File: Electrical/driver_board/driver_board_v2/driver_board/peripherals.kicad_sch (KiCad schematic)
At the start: 16 parts, among them J10 Conn_01x02_Socket, J11 Conn_01x06_Pin

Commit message: Value assignment and protection for driver board
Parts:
- renumbered C43 to C44, C44 to C45, C45 to C46, C46 to C47, C47 to C48, C48 to C49, C49 to C50, C50 to C51, J11 to J10, J10 to J11

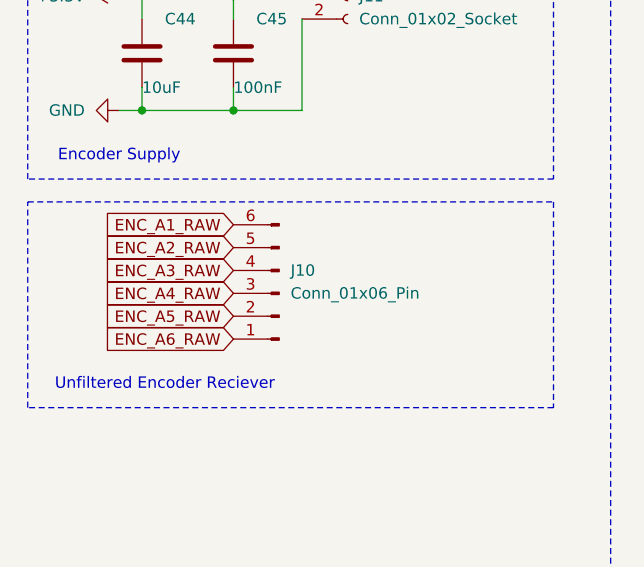
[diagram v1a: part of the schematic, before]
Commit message: Improved routing
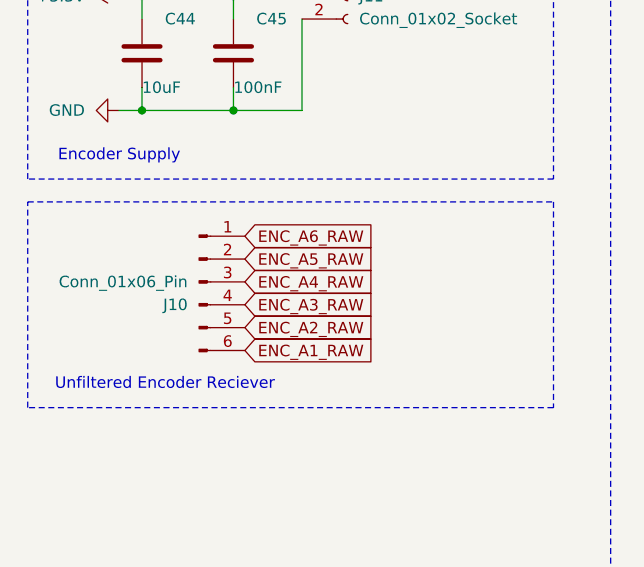
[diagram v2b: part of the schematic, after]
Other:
- moved on the sheet: J10
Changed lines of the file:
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@@
 	(global_label "ENC_A5_RAW"
 		(shape input)
-		(at 63.5 68.58 180)
+		(at 64.77 62.23 0)
 		(fields_autoplaced yes)
 		(effects
@@
 				(size 1.27 1.27)
 			)
-			(justify right)
+			(justify left)
 		)
 		(property "Intersheetrefs" "${INTERSHEET_REFS}"
-			(at 48.722 68.58 0)
-			(hide yes)
-			(show_name no)
-			(do_not_autoplace no)
-			(effects
-				(font
-					(size 1.27 1.27)
-				)
-				(justify right)
+			(at 79.548 62.23 0)
+			(hide yes)
+			(show_name no)
+			(do_not_autoplace no)
+			(effects
+				(font
+					(size 1.27 1.27)
+				)
+				(justify left)
 			)
 		)
@@
 	(global_label "ENC_A2_RAW"
 		(shape input)
-		(at 63.5 60.96 180)
+		(at 64.77 69.85 0)
 		(fields_autoplaced yes)
 		(effects
@@
 				(size 1.27 1.27)
 			)
-			(justify right)
+			(justify left)
 		)
 		(property "Intersheetrefs" "${INTERSHEET_REFS}"
-			(at 48.722 60.96 0)
-			(hide yes)
-			(show_name no)
-			(do_not_autoplace no)
-			(effects
-				(font
-					(size 1.27 1.27)
-				)
-				(justify right)
+			(at 79.548 69.85 0)
+			(hide yes)
+			(show_name no)
+			(do_not_autoplace no)
+			(effects
+				(font
+					(size 1.27 1.27)
+				)
+				(justify left)
 			)
 		)
@@
 	(global_label "ENC_A1_RAW"
 		(shape input)
-		(at 63.5 58.42 180)
+		(at 64.77 72.39 0)
 		(fields_autoplaced yes)
 		(effects
@@
 				(size 1.27 1.27)
 			)
-			(justify right)
+			(justify left)
 		)
 		(property "Intersheetrefs" "${INTERSHEET_REFS}"
-			(at 48.722 58.42 0)
-			(hide yes)
-			(show_name no)
-			(do_not_autoplace no)
-			(effects
-				(font
-					(size 1.27 1.27)
-				)
-				(justify right)
+			(at 79.548 72.39 0)
+			(hide yes)
+			(show_name no)
+			(do_not_autoplace no)
+			(effects
+				(font
+					(size 1.27 1.27)
+				)
+				(justify left)
 			)
 		)
@@
 	(global_label "ENC_A4_RAW"
 		(shape input)
-		(at 63.5 66.04 180)
+		(at 64.77 64.77 0)
 		(fields_autoplaced yes)
 		(effects
@@
 				(size 1.27 1.27)
 			)
-			(justify right)
+			(justify left)
 		)
 		(property "Intersheetrefs" "${INTERSHEET_REFS}"
-			(at 48.722 66.04 0)
-			(hide yes)
-			(show_name no)
-			(do_not_autoplace no)
-			(effects
-				(font
-					(size 1.27 1.27)
-				)
-				(justify right)
+			(at 79.548 64.77 0)
+			(hide yes)
+			(show_name no)
+			(do_not_autoplace no)
+			(effects
+				(font
+					(size 1.27 1.27)
+				)
+				(justify left)
 			)
 		)
@@
 	(global_label "ENC_A3_RAW"
 		(shape input)
-		(at 63.5 63.5 180)
+		(at 64.77 67.31 0)
 		(fields_autoplaced yes)
 		(effects
@@
 				(size 1.27 1.27)
 			)
-			(justify right)
+			(justify left)
 		)
 		(property "Intersheetrefs" "${INTERSHEET_REFS}"
-			(at 48.722 63.5 0)
-			(hide yes)
-			(show_name no)
-			(do_not_autoplace no)
-			(effects
-				(font
-					(size 1.27 1.27)
-				)
-				(justify right)
+			(at 79.548 67.31 0)
+			(hide yes)
+			(show_name no)
+			(do_not_autoplace no)
+			(effects
+				(font
+					(size 1.27 1.27)
+				)
+				(justify left)
 			)
 		)
@@
 	(global_label "ENC_A6_RAW"
 		(shape input)
-		(at 63.5 71.12 180)
+		(at 64.77 59.69 0)
 		(fields_autoplaced yes)
 		(effects
@@
 				(size 1.27 1.27)
 			)
-			(justify right)
+			(justify left)
 		)
 		(property "Intersheetrefs" "${INTERSHEET_REFS}"
-			(at 48.722 71.12 0)
-			(hide yes)
-			(show_name no)
-			(do_not_autoplace no)
-			(effects
-				(font
-					(size 1.27 1.27)
-				)
-				(justify right)
+			(at 79.548 59.69 0)
+			(hide yes)
+			(show_name no)
+			(do_not_autoplace no)
+			(effects
+				(font
+					(size 1.27 1.27)
+				)
+				(justify left)
 			)
 		)
@@
 	(symbol
 		(lib_id "Connector:Conn_01x06_Pin")
-		(at 68.58 66.04 180)
+		(at 59.69 64.77 0)
 		(unit 1)
 		(body_style 1)
@@
 		(fields_autoplaced yes)
 		(property "Reference" "J10"
-			(at 69.85 63.4999 0)
+			(at 58.42 67.3101 0)
 			(show_name no)
 			(do_not_autoplace no)
@@
 		)
 		(property "Value" "Conn_01x06_Pin"
-			(at 69.85 66.0399 0)
+			(at 58.42 64.7701 0)
 			(show_name no)
 			(do_not_autoplace no)
@@
 		)
 		(property "Footprint" ""
-			(at 68.58 66.04 0)
+			(at 59.69 64.77 0)
 			(hide yes)
 			(show_name no)
@@
 		)
 		(property "Datasheet" ""
-			(at 68.58 66.04 0)
+			(at 59.69 64.77 0)
 			(hide yes)
 			(show_name no)
@@
 		)
 		(property "Description" "Generic connector, single row, 01x06, script generated"
-			(at 68.58 66.04 0)
-			(hide yes)
-			(show_name no)
+			(at 59.69 64.77 0)
+			(hide yes)
+			(show_name no)

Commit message: Added new converter
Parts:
- renumbered C44 to C39, C45 to C40, C46 to C41, C47 to C42, C48 to C43, C49 to C44, C50 to C45, C51 to C46, R13 to R10, R14 to R11, R15 to R12, R16 to R13, R11 to R8, R12 to R9
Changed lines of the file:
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@@
 		(dnp no)
 		(fields_autoplaced yes)
-		(property "Reference" "R15"
+		(property "Reference" "R12"
 			(at 132.08 125.73 90)
 			(show_name no)
@@
 			(project "driver_board"
 				(path "/914a9dfd-cc72-459d-a4b5-1249c31e6215/1d053789-bb06-47b5-b093-e7b74b4d3277"
-					(reference "R15")
+					(reference "R12")
 					(unit 1)
 				)
@@
 		(dnp no)
 		(fields_autoplaced yes)
-		(property "Reference" "C48"
+		(property "Reference" "C43"
 			(at 142.24 91.4399 0)
 			(show_name no)
@@
 			(project "driver_board"
 				(path "/914a9dfd-cc72-459d-a4b5-1249c31e6215/1d053789-bb06-47b5-b093-e7b74b4d3277"
-					(reference "C48")
+					(reference "C43")
 					(unit 1)
 				)
@@
 		(dnp no)
 		(fields_autoplaced yes)
-		(property "Reference" "C50"
+		(property "Reference" "C45"
 			(at 142.24 137.1599 0)
 			(show_name no)
@@
 			(project "driver_board"
 				(path "/914a9dfd-cc72-459d-a4b5-1249c31e6215/1d053789-bb06-47b5-b093-e7b74b4d3277"
-					(reference "C50")
+					(reference "C45")
 					(unit 1)
 				)
@@
 		(in_pos_files yes)
 		(dnp no)
-		(property "Reference" "C45"
+		(property "Reference" "C40"
 			(at 66.04 35.56 0)
 			(show_name no)
@@
 			(project "driver_board"
 				(path "/914a9dfd-cc72-459d-a4b5-1249c31e6215/1d053789-bb06-47b5-b093-e7b74b4d3277"
-					(reference "C45")
+					(reference "C40")
 					(unit 1)
 				)
@@
 		(dnp no)
 		(fields_autoplaced yes)
-		(property "Reference" "#PWR065"
+		(property "Reference" "#PWR067"
 			(at 54.61 33.02 0)
 			(hide yes)
@@
 			(project "driver_board"
 				(path "/914a9dfd-cc72-459d-a4b5-1249c31e6215/1d053789-bb06-47b5-b093-e7b74b4d3277"
-					(reference "#PWR065")
+					(reference "#PWR067")
 					(unit 1)
 				)
@@
 		(dnp no)
 		(fields_autoplaced yes)
-		(property "Reference" "R16"
+		(property "Reference" "R13"
 			(at 132.08 148.59 90)
 			(show_name no)
@@
 			(project "driver_board"
 				(path "/914a9dfd-cc72-459d-a4b5-1249c31e6215/1d053789-bb06-47b5-b093-e7b74b4d3277"
-					(reference "R16")
+					(reference "R13")
 					(unit 1)
 				)
@@
 		(dnp no)
 		(fields_autoplaced yes)
-		(property "Reference" "R13"
+		(property "Reference" "R10"
 			(at 132.08 80.01 90)
 			(show_name no)
@@
 			(project "driver_board"
 				(path "/914a9dfd-cc72-459d-a4b5-1249c31e6215/1d053789-bb06-47b5-b093-e7b74b4d3277"
-					(reference "R13")
+					(reference "R10")
 					(unit 1)
 				)
@@
 		(in_pos_files yes)
 		(dnp no)
-		(property "Reference" "C44"
+		(property "Reference" "C39"
 			(at 55.88 35.56 0)
 			(show_name no)
@@
 			(project "driver_board"
 				(path "/914a9dfd-cc72-459d-a4b5-1249c31e6215/1d053789-bb06-47b5-b093-e7b74b4d3277"
-					(reference "C44")
+					(reference "C39")
 					(unit 1)
 				)
@@
 		(dnp no)
 		(fields_autoplaced yes)
-		(property "Reference" "#PWR072"
+		(property "Reference" "#PWR074"
 			(at 138.43 173.99 0)
 			(hide yes)
@@
 			(project "driver_board"
 				(path "/914a9dfd-cc72-459d-a4b5-1249c31e6215/1d053789-bb06-47b5-b093-e7b74b4d3277"
-					(reference "#PWR072")
+					(reference "#PWR074")
 					(unit 1)
 				)
@@
 		(dnp no)
 		(fields_autoplaced yes)
-		(property "Reference" "#PWR067"
+		(property "Reference" "#PWR069"
 			(at 138.43 59.69 0)
 			(hide yes)
@@
 			(project "driver_board"
 				(path "/914a9dfd-cc72-459d-a4b5-1249c31e6215/1d053789-bb06-47b5-b093-e7b74b4d3277"
-					(reference "#PWR067")
+					(reference "#PWR069")
 					(unit 1)
 				)
@@
 		(dnp no)
 		(fields_autoplaced yes)
-		(property "Reference" "R12"
+		(property "Reference" "R9"
 			(at 132.08 57.15 90)
 			(show_name no)
@@
 			(project "driver_board"
 				(path "/914a9dfd-cc72-459d-a4b5-1249c31e6215/1d053789-bb06-47b5-b093-e7b74b4d3277"
-					(reference "R12")
+					(reference "R9")
 					(unit 1)
 				)
@@
 		(dnp no)
 		(fields_autoplaced yes)
-		(property "Reference" "#PWR070"
+		(property "Reference" "#PWR072"
 			(at 138.43 128.27 0)
 			(hide yes)
@@
 			(project "driver_board"
 				(path "/914a9dfd-cc72-459d-a4b5-1249c31e6215/1d053789-bb06-47b5-b093-e7b74b4d3277"
-					(reference "#PWR070")
+					(reference "#PWR072")
 					(unit 1)
 				)
@@
 		(dnp no)
 		(fields_autoplaced yes)
-		(property "Reference" "R11"
+		(property "Reference" "R8"
 			(at 132.08 34.29 90)
 			(show_name no)
@@
 			(project "driver_board"
 				(path "/914a9dfd-cc72-459d-a4b5-1249c31e6215/1d053789-bb06-47b5-b093-e7b74b4d3277"
-					(reference "R11")
+					(reference "R8")
 					(unit 1)
 				)
@@
 		(dnp no)
 		(fields_autoplaced yes)
-		(property "Reference" "#PWR069"
+		(property "Reference" "#PWR071"
 			(at 138.43 105.41 0)
 			(hide yes)
@@
 			(project "driver_board"
 				(path "/914a9dfd-cc72-459d-a4b5-1249c31e6215/1d053789-bb06-47b5-b093-e7b74b4d3277"
-					(reference "#PWR069")
+					(reference "#PWR071")
 					(unit 1)
 				)
@@
 		(dnp no)
 		(fields_autoplaced yes)
-		(property "Reference" "#PWR071"
+		(property "Reference" "#PWR073"
 			(at 138.43 151.13 0)
 			(hide yes)
@@
 			(project "driver_board"
 				(path "/914a9dfd-cc72-459d-a4b5-1249c31e6215/1d053789-bb06-47b5-b093-e7b74b4d3277"
-					(reference "#PWR071")
+					(reference "#PWR073")
 					(unit 1)
 				)
@@
 		(dnp no)
 		(fields_autoplaced yes)
-		(property "Reference" "C49"
+		(property "Reference" "C44"
 			(at 142.24 114.2999 0)
 			(show_name no)
@@
 			(project "driver_board"
 				(path "/914a9dfd-cc72-459d-a4b5-1249c31e6215/1d053789-bb06-47b5-b093-e7b74b4d3277"
-					(reference "C49")
+					(reference "C44")
 					(unit 1)
 				)
@@
 		(dnp no)
 		(fields_autoplaced yes)
-		(property "Reference" "C51"
+		(property "Reference" "C46"
 			(at 142.24 160.0199 0)
 			(show_name no)
@@
 			(project "driver_board"
 				(path "/914a9dfd-cc72-459d-a4b5-1249c31e6215/1d053789-bb06-47b5-b093-e7b74b4d3277"
-					(reference "C51")
+					(reference "C46")
 					(unit 1)
 				)
@@
 		(dnp no)
 		(fields_autoplaced yes)
-		(property "Reference" "C47"
+		(property "Reference" "C42"
 			(at 142.24 68.5799 0)
 			(show_name no)
@@
 			(project "driver_board"
 				(path "/914a9dfd-cc72-459d-a4b5-1249c31e6215/1d053789-bb06-47b5-b093-e7b74b4d3277"
-					(reference "C47")
+					(reference "C42")
 					(unit 1)
 				)
@@
 		(dnp no)
 		(fields_autoplaced yes)
-		(property "Reference" "C46"
+		(property "Reference" "C41"
 			(at 142.24 45.7199 0)
 			(show_name no)
@@
 			(project "driver_board"
 				(path "/914a9dfd-cc72-459d-a4b5-1249c31e6215/1d053789-bb06-47b5-b093-e7b74b4d3277"
-					(reference "C46")
+					(reference "C41")
 					(unit 1)
 				)
@@
 		(dnp no)
 		(fields_autoplaced yes)
-		(property "Reference" "#PWR066"
+		(property "Reference" "#PWR068"
 			(at 44.45 45.72 0)
 			(hide yes)
@@
 			(project "driver_board"
 				(path "/914a9dfd-cc72-459d-a4b5-1249c31e6215/1d053789-bb06-47b5-b093-e7b74b4d3277"
-					(reference "#PWR066")
+					(reference "#PWR068")
 					(unit 1)
 				)
@@
 		(dnp no)
 		(fields_autoplaced yes)
-		(property "Reference" "#PWR068"
+		(property "Reference" "#PWR070"
 			(at 138.43 82.55 0)
 			(hide yes)
@@
 			(project "driver_board"
 				(path "/914a9dfd-cc72-459d-a4b5-1249c31e6215/1d053789-bb06-47b5-b093-e7b74b4d3277"
-					(reference "#PWR068")
+					(reference "#PWR070")
 					(unit 1)
 				)
@@
 		(dnp no)
 		(fields_autoplaced yes)
-		(property "Reference" "R14"
+		(property "Reference" "R11"
 			(at 132.08 102.87 90)
 			(show_name no)
@@
 			(project "driver_board"
 				(path "/914a9dfd-cc72-459d-a4b5-1249c31e6215/1d053789-bb06-47b5-b093-e7b74b4d3277"
-					(reference "R14")
-					(unit 1)
-				)
+					(reference "R11")
+					(unit 1)
+				)
